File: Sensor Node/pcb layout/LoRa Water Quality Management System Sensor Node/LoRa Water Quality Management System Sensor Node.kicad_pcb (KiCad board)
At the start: 4 copper layers, 100 x 75 mm, 121 parts, among them J1 PxC 1757255, J10 Conn_01x03, J2 PxC 1757242, J3 Conn_Coaxial, J4 PxC 1757255, J5 PxC 1757255, J6 Conn_01x02, J7 USB_B, J8 SMA-J-P-X-RA-TH1, J9 Conn_01x02, SW1 Tactile Pushbutton, U1 TMUX1309, U10 TPS631010YBGR, U11 LMV324, U12 MCP4651T-503E/ML, U13 MCP4651T-503E/ML, U2 LSF0102, U3 TMUX1309, U4 Core1262 HF, U5 MX25L3233FM2I-08Q, U6 MCP3425Axx-xCH, U7 W25Q128JVSIQ TR, U8 RP2350_60QFN, U9 TPS631010YBGR, Y1 ABM8-272-T3

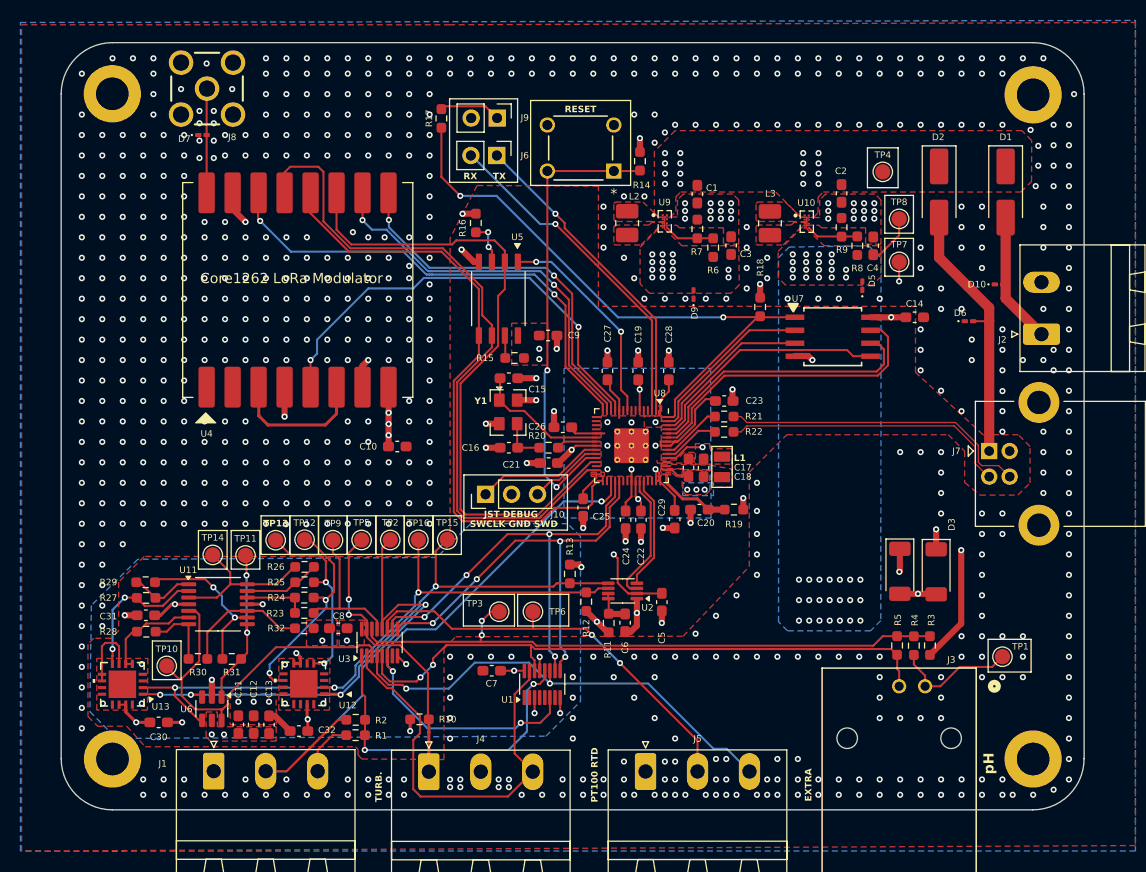
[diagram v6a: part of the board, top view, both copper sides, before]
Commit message: Resolve JLCPCB DFM issues
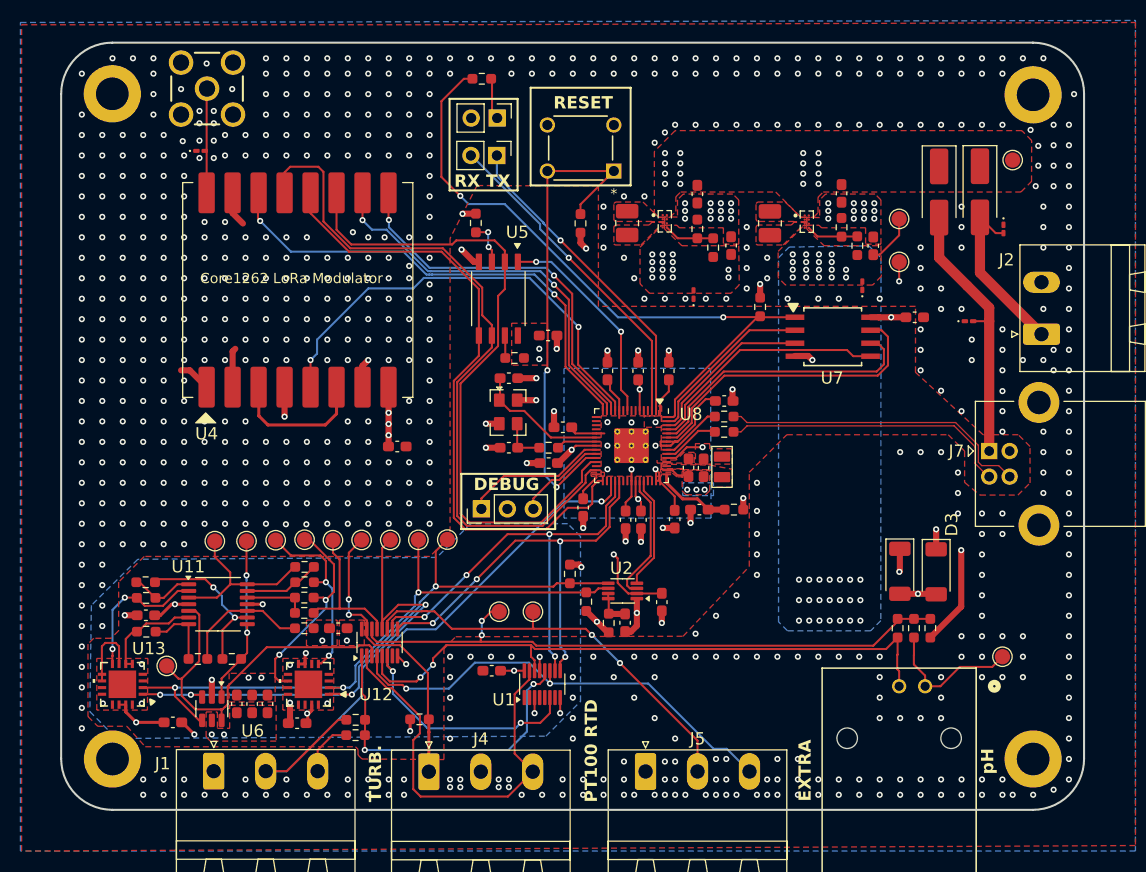
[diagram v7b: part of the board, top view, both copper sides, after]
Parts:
- added G***: LOGO, LWQMS:psh, F.Cu at (178.6, 69.6)
- moved TP4 12.8 mm to (193.5, 36.9)
- moved R14 8.41 mm to (151.2, 43.1), turned to 90 degrees
- moved R17 5.54 mm to (141.6, 29.0), turned to 180 degrees
- moved D10 5.43 mm to (192.6, 43.7), turned to -90 degrees
- moved D1 2.51 mm to (190.3, 40.0)
- moved C13 2.04 mm to (120.6, 90.1)
- moved C11 2.03 mm to (117.6, 90.1)
- moved C12 2.03 mm to (119.1, 90.1)
- moved R4 1.71 mm to (183.8, 82.7)
- moved R3 1.70 mm to (185.4, 82.7)
- moved R5 1.69 mm to (182.2, 82.7)
- moved D7 1.56 mm to (114.1, 36.0)
- moved J10 1.49 mm to (141.5, 71.0)
- moved TP11 1.40 mm to (118.6, 74.2)
- moved C30 1.39 mm to (111.4, 91.9)
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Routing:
- net GND: track 56.2 -> 64.5 mm, vias 778 -> 771
- net /MCU/QSPI_SS: track 59.1 -> 65.6 mm
- net /V_{BATT}: track 12.9 -> 16.9 mm
- net /MCU/~{RESET}: track 45.6 -> 48.7 mm
- net /PH_GND: track 60.4 -> 62.4 mm
- net Net-(J9-Pin_1): track 6.04 -> 4.08 mm
- net /PH_RAW: track 12.3 -> 14.0 mm
- net /MCU/SWD: track 7.38 -> 8.98 mm
- net /MCU/SWCLK: track 12.6 -> 14.2 mm
- net /SPI_MISO_{0}: track 63.9 -> 65.5 mm
- net /Software-Defined Instrumentation Amplifier/OUT: track 15.8 -> 17.1 mm
- net /SPI_SCK_{0}: track 68.8 -> 70.1 mm
- net /I2C_SCL_{1}_5V: track 58.7 -> 60.0 mm
- net /Software-Defined Instrumentation Amplifier/V_SENSOR_WITH_DC_OFFSET: track 15.1 -> 16.4 mm
- net +3V3: track 74.3 -> 73.1 mm
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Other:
- board text added: "DEBUG"
- board text added: "LWQMS Node"
- board text added: "Yet another groundbreaking project by Matthew Sharp, Cole Hadley, and Patricio Palermo"
- board text removed: "JST DEBUG"
- board text removed: "SWCLK GND SWD"

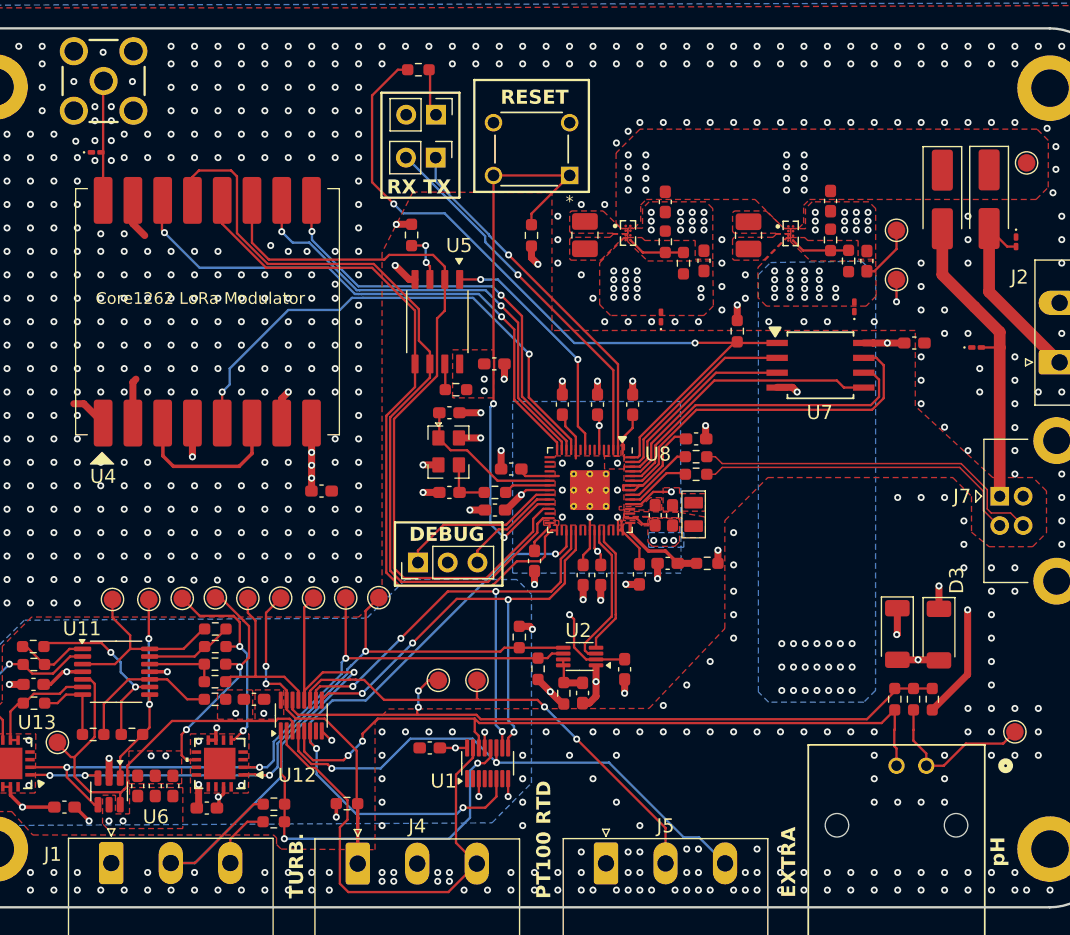
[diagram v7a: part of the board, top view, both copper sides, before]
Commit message: Add indicator LEDs, PCB cleanup, and preliminary BOM, assuming R/C can be sourced from equipment room.
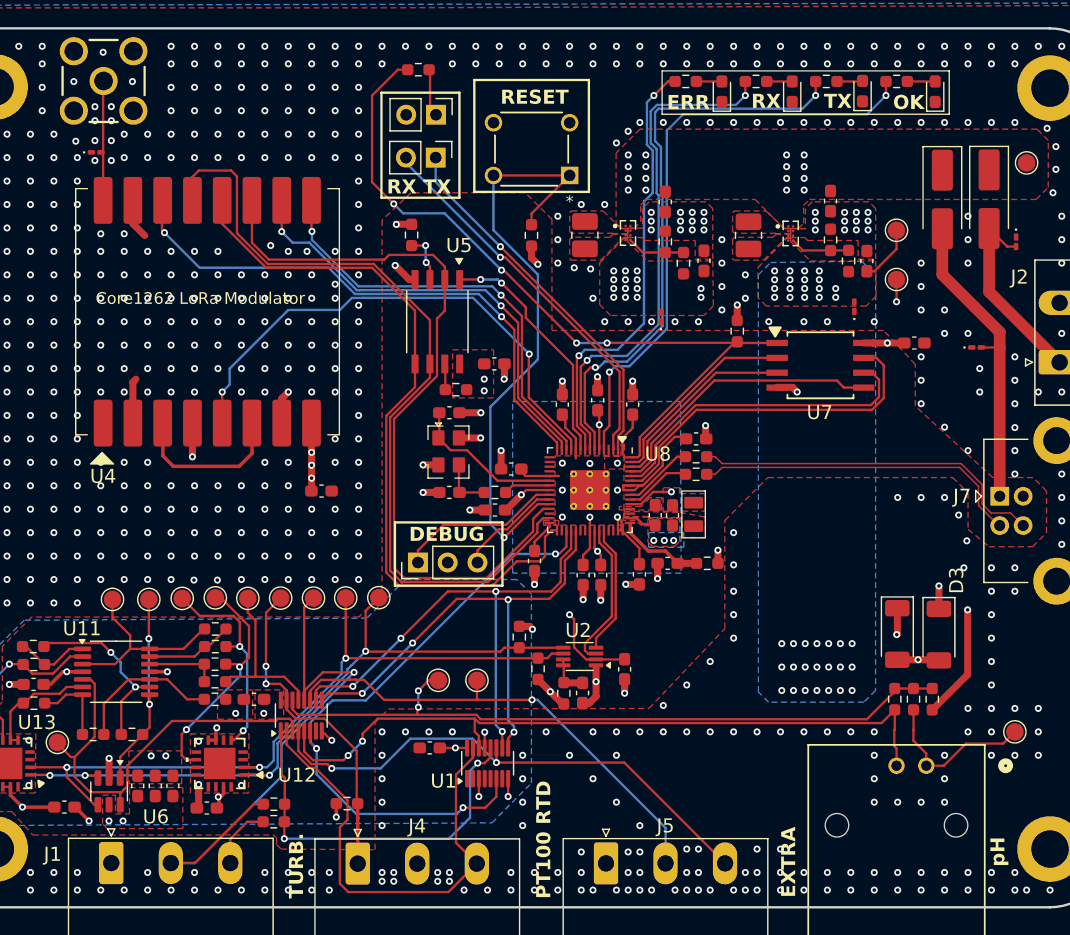
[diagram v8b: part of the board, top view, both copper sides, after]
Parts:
- added D11: LED, LED_SMD:LED_0603_1608Metric_Pad1.05x0.95mm_HandSolder, F.Cu at (173.5, 30.9)
- added D12: LED, LED_SMD:LED_0603_1608Metric_Pad1.05x0.95mm_HandSolder, F.Cu at (179.5, 30.8)
- added D13: LED, LED_SMD:LED_0603_1608Metric_Pad1.05x0.95mm_HandSolder, F.Cu at (185.7, 30.9)
- added D8: LED, LED_SMD:LED_0603_1608Metric_Pad1.05x0.95mm_HandSolder, F.Cu at (167.5, 30.9)
- added R33: 70R, Resistor_SMD:R_0603_1608Metric_Pad0.98x0.95mm_HandSolder, F.Cu at (164.4, 30.0)
- added R34: 160R, Resistor_SMD:R_0603_1608Metric_Pad0.98x0.95mm_HandSolder, F.Cu at (170.4, 30.0)
- added R35: 160R, Resistor_SMD:R_0603_1608Metric_Pad0.98x0.95mm_HandSolder, F.Cu at (176.4, 30.0)
- added R36: 160R, Resistor_SMD:R_0603_1608Metric_Pad0.98x0.95mm_HandSolder, F.Cu at (182.4, 30.0)
- moved C19 0.37 mm to (156.9, 57.2)
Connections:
- U8 pad 10: /MCU/GPIO7 -> /~{FLASH_CS}
- U8 pad 5: /MCU/GPIO3 -> /STATUS_LED
- U8 pad 7: /MCU/GPIO4 -> /TX_LED
- U8 pad 8: /MCU/GPIO5 -> /RX_LED
- U8 pad 9: /~{FLASH_CS} -> /ERR_LED
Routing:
- net /STATUS_LED: track 0.00 -> 51.3 mm, vias 0 -> 2
- net /TX_LED: track 0.00 -> 49.2 mm, vias 0 -> 2
- net /RX_LED: track 0.00 -> 43.8 mm, vias 0 -> 2
- net /ERR_LED: track 0.00 -> 37.6 mm, vias 0 -> 2
- net GND: track 64.5 -> 61.3 mm, vias 771 -> 772
- net /MCU/~{RESET}: track 48.7 -> 51.8 mm, vias 2 -> 1
- net Net-(D13-A): track 0.00 -> 2.38 mm
- net Net-(D12-A): track 0.00 -> 2.22 mm
- net Net-(D8-A): track 0.00 -> 2.18 mm
- net Net-(D11-A): track 0.00 -> 2.18 mm
- net /UART_RX_{0}: track 32.3 -> 32.9 mm
- net +1V1: track 14.4 -> 15.0 mm
- net /MCU/QSPI_SS: track 65.6 -> 65.8 mm, vias 2 -> 4
- net /EXTRA_IN: vias 2 -> 1
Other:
- board text added: "ERR"
- board text added: "OK"
- board text added: "RX"
- board text added: "TX"
